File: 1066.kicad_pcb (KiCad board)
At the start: 2 copper layers, 228.6 x 139.7 mm, 83 parts, among them J1 Conn_01x03, P1 Conn_01x50_Male_Atari_1066, P2 Conn_01x40_Male, SW1 Bank, U1 74LS156, U10 4164, U11 4164, U12 74LS157, U13 74LS257, U14 74LS257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

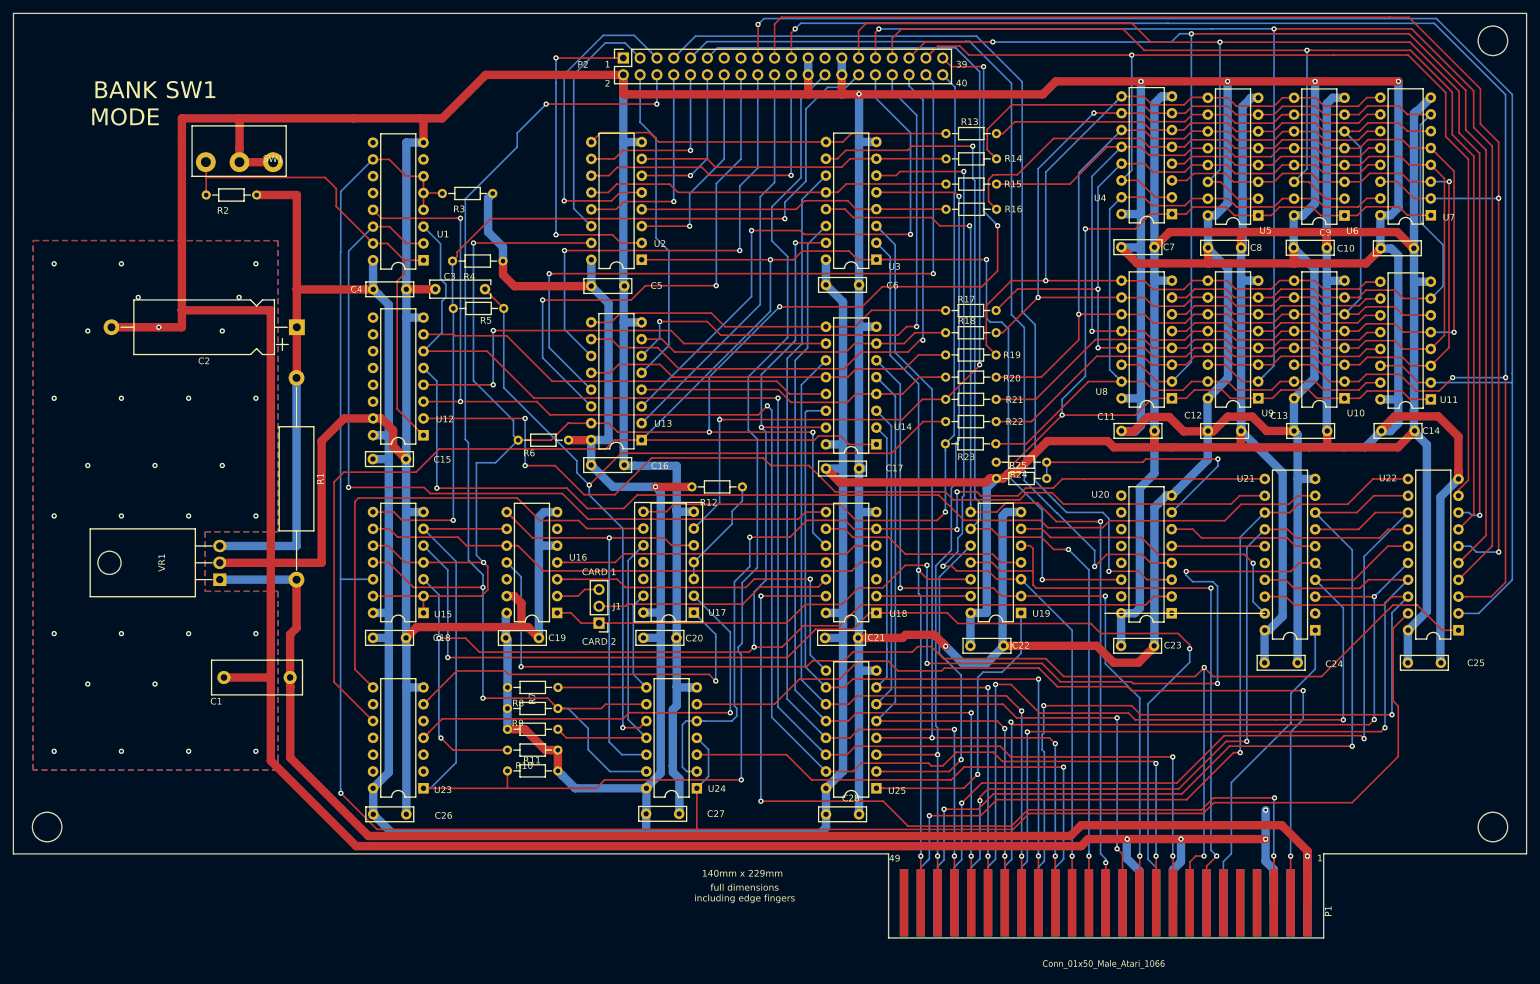
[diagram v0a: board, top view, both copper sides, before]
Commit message: fixed lower trace  by C11
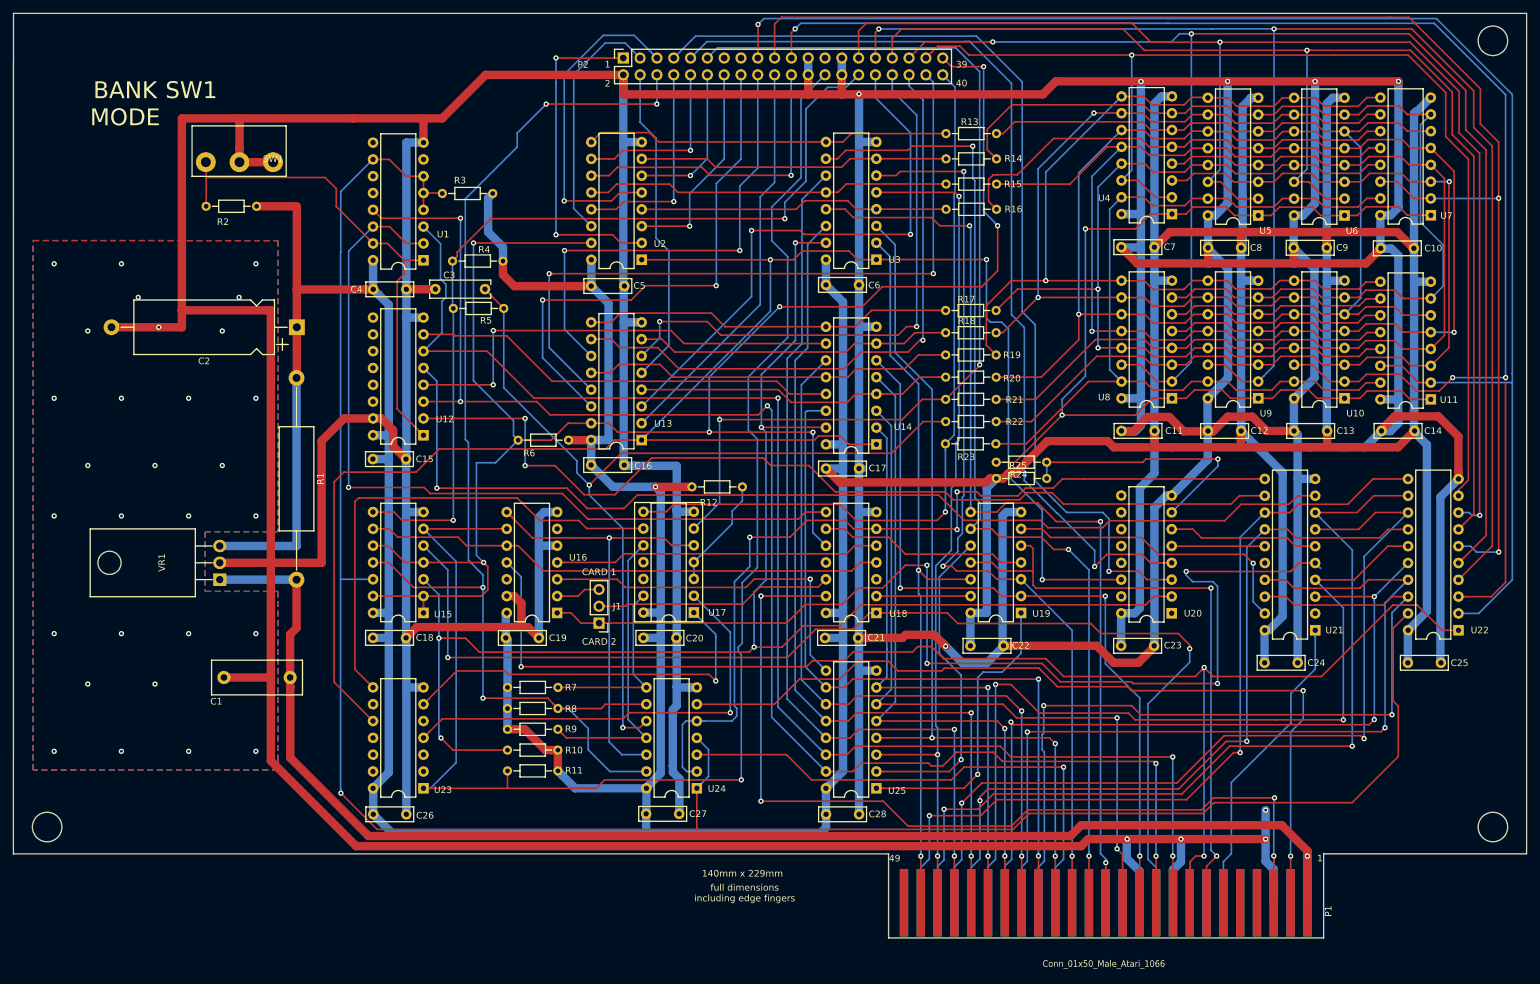
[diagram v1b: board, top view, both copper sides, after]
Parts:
- moved R2 1.70 mm to (73.8, 54.8)
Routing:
- net VCC: track 1040.5 -> 1038.8 mm
- net Net-(R2-Pad2): track 73.1 -> 74.9 mm
